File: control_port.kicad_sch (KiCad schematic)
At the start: 14 parts, among them J2 USB_C, U16 PI3USB102G

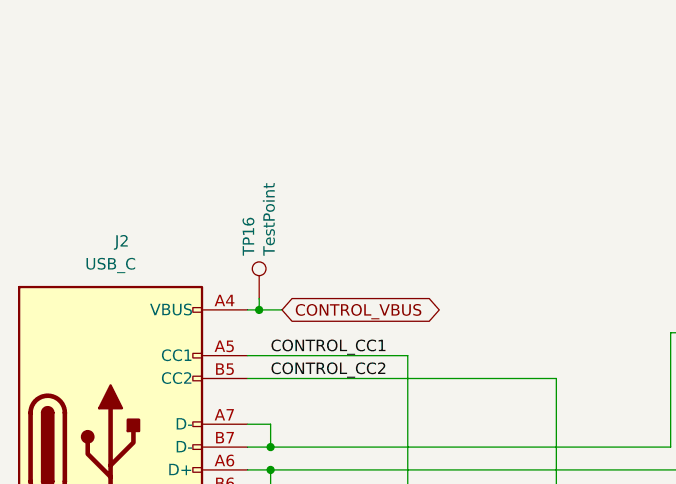
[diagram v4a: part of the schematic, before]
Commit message: Use four-terminal current sense resistor symbol
Previously we had used a special four-terminal symbol and footprint to
ensure that current sense signals did not connect to power supply zones
in multiple places. We rejected this in favor of a two-terminal
schematic symbol and standard resistor footprint to ensure reliable
assembly.

This new solution uses a four-terminal schematic symbol with a
two-terminal footprint which is actually four terminals in two
overlapping pairs using the "net tie" footprint feature.

Fixes #13
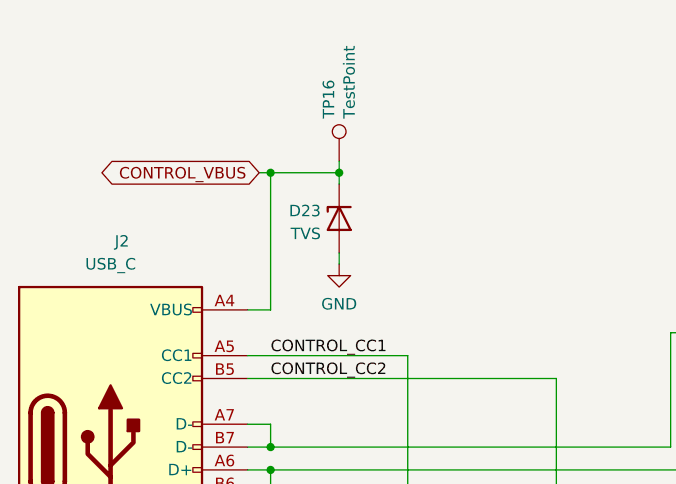
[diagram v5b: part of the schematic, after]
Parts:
- added D23: TVS, cynthion:DFN1006-2, symbol Device:D_Zener
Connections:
- net CONTROL_VBUS: now also D23.1 (K)
- net GND: now also D23.2 (A)
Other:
- moved on the sheet: TP16
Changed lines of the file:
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@@
   (junction (at 77.47 87.63) (diameter 0) (color 0 0 0 0)
   )
+  (junction (at 85.09 54.61) (diameter 0) (color 0 0 0 0)
+  )
   (junction (at 92.71 105.41) (diameter 0) (color 0 0 0 0)
   )
@@
   (junction (at 109.22 105.41) (diameter 0) (color 0 0 0 0)
   )
-  (junction (at 76.2 69.85) (diameter 0) (color 0 0 0 0)
+  (junction (at 77.47 54.61) (diameter 0) (color 0 0 0 0)
   )
   (no_connect (at 74.93 100.33))
@@
     (stroke (width 0) (type default))
   )
-  (wire (pts (xy 76.2 68.58) (xy 76.2 69.85))
+  (wire (pts (xy 77.47 69.85) (xy 74.93 69.85))
+    (stroke (width 0) (type default))
+  )
+  (wire (pts (xy 77.47 54.61) (xy 77.47 69.85))
     (stroke (width 0) (type default))
   )
@@
     (stroke (width 0) (type default))
   )
-  (wire (pts (xy 76.2 69.85) (xy 78.74 69.85))
-    (stroke (width 0) (type default))
-  )
   (wire (pts (xy 231.14 62.23) (xy 231.14 63.5))
     (stroke (width 0) (type default))
@@
     (stroke (width 0) (type default))
   )
-  (wire (pts (xy 74.93 69.85) (xy 76.2 69.85))
-    (stroke (width 0) (type default))
-  )
   (wire (pts (xy 92.71 95.25) (xy 92.71 92.71))
     (stroke (width 0) (type default))
@@
     (stroke (width 0) (type default))
   )
+  (wire (pts (xy 76.2 54.61) (xy 77.47 54.61))
+    (stroke (width 0) (type default))
+  )
   (wire (pts (xy 259.08 81.28) (xy 259.08 82.55))
     (stroke (width 0) (type default))
@@
     (stroke (width 0) (type default))
   )
+  (wire (pts (xy 85.09 64.77) (xy 85.09 63.5))
+    (stroke (width 0) (type default))
+  )
   (wire (pts (xy 198.12 77.47) (xy 199.39 77.47))
     (stroke (width 0) (type default))
   )
+  (wire (pts (xy 77.47 54.61) (xy 85.09 54.61))
+    (stroke (width 0) (type default))
+  )
   (wire (pts (xy 92.71 74.93) (xy 92.71 92.71))
     (stroke (width 0) (type default))
@@
     (stroke (width 0) (type default))
   )
+  (wire (pts (xy 85.09 53.34) (xy 85.09 54.61))
+    (stroke (width 0) (type default))
+  )
   (wire (pts (xy 208.28 129.54) (xy 208.28 130.81))
     (stroke (width 0) (type default))
@@
   )
   (wire (pts (xy 173.99 80.01) (xy 173.99 113.03))
+    (stroke (width 0) (type default))
+  )
+  (wire (pts (xy 85.09 54.61) (xy 85.09 55.88))
     (stroke (width 0) (type default))
   )
@@
     (effects (font (size 1.27 1.27)) (justify left bottom))
   )
-  (global_label "CONTROL_VBUS" (shape bidirectional) (at 78.74 69.85 0) (fields_autoplaced)
-    (effects (font (size 1.27 1.27)) (justify left))
-    (property "Intersheetrefs" "${INTERSHEET_REFS}" (at 95.4575 69.7706 0)
-      (effects (font (size 1.27 1.27)) (justify left) hide)
+  (global_label "CONTROL_VBUS" (shape bidirectional) (at 76.2 54.61 180) (fields_autoplaced)
+    (effects (font (size 1.27 1.27)) (justify right))
+    (property "Intersheetrefs" "${INTERSHEET_REFS}" (at 58.5231 54.61 0)
+      (effects (font (size 1.27 1.27)) (justify right) hide)
     )
   )
@@
         (path "/fb621148-8145-4217-9712-738e1b5a4823/00000000-0000-0000-0000-00005dcd9772"
           (reference "C62") (unit 1)
+        )
+      )
+    )
+  )
+  (symbol (lib_id "Device:D_Zener") (at 85.09 59.69 90) (mirror x) (unit 1)
+    (in_bom yes) (on_board yes) (dnp no) (fields_autoplaced)
+    (property "Reference" "D23" (at 83.058 58.8553 90)
+      (effects (font (size 1.27 1.27)) (justify left))
+    )
+    (property "Value" "TVS" (at 83.058 61.3922 90)
+      (effects (font (size 1.27 1.27)) (justify left))
+    )
+    (property "Footprint" "cynthion:DFN1006-2" (at 85.09 59.69 0)
+      (effects (font (size 1.27 1.27)) hide)
+    )
+    (property "Datasheet" "https://assets.nexperia.com/documents/data-sheet/PESDXS1UL_SER.pdf" (at 85.09 59.69 0)
+      (effects (font (size 1.27 1.27)) hide)
+    )
+    (property "Manufacturer" "Nexperia" (at 85.09 59.69 90)
+      (effects (font (size 1.27 1.27)) hide)
+    )
+    (property "Part Number" "PESD36VS1UL,315" (at 85.09 59.69 90)
+      (effects (font (size 1.27 1.27)) hide)
+    )
+    (property "Description" "TVS DIODE 36VWM 80VC DFN1006-2" (at 85.09 59.69 0)
+      (effects (font (size 1.27 1.27)) hide)
+    )
+    (pin "1")
+    (pin "2")
+    (instances
+      (project "cynthion"
+        (path "/fb621148-8145-4217-9712-738e1b5a4823/490fda6e-4eae-4b35-a875-405b51914829"
+          (reference "D23") (unit 1)
+        )
+        (path "/fb621148-8145-4217-9712-738e1b5a4823/00000000-0000-0000-0000-00005dcd9772"
+          (reference "D23") (unit 1)
         )
       )
@@
     )
   )
-  (symbol (lib_id "Connector:TestPoint") (at 76.2 68.58 0) (unit 1)
+  (symbol (lib_id "Connector:TestPoint") (at 85.09 53.34 0) (unit 1)
     (in_bom no) (on_board yes) (dnp no)
-    (property "Reference" "TP16" (at 75.057 63.8302 90)
-      (effects (font (size 1.27 1.27)) (justify left))
-    )
-    (property "Value" "TestPoint" (at 77.343 63.8302 90)
-      (effects (font (size 1.27 1.27)) (justify left))
-    )
-    (property "Footprint" "TestPoint:TestPoint_Pad_D1.0mm" (at 81.28 68.58 0)
-      (effects (font (size 1.27 1.27)) hide)
-    )
-    (property "Datasheet" "~" (at 81.28 68.58 0)
+    (property "Reference" "TP16" (at 83.947 48.5902 90)
+      (effects (font (size 1.27 1.27)) (justify left))
+    )
+    (property "Value" "TestPoint" (at 86.233 48.5902 90)
+      (effects (font (size 1.27 1.27)) (justify left))
+    )
+    (property "Footprint" "TestPoint:TestPoint_Pad_D1.0mm" (at 90.17 53.34 0)
+      (effects (font (size 1.27 1.27)) hide)
+    )
+    (property "Datasheet" "~" (at 90.17 53.34 0)
       (effects (font (size 1.27 1.27)) hide)
     )
@@
         )
       )
+    )
+  )
+  (symbol (lib_id "power:GND") (at 85.09 64.77 0) (unit 1)
+    (in_bom yes) (on_board yes) (dnp no) (fields_autoplaced)
+    (property "Reference" "#PWR025" (at 85.09 71.12 0)
+      (effects (font (size 1.27 1.27)) hide)
+    )
+    (property "Value" "GND" (at 85.09 69.2134 0)
+      (effects (font (size 1.27 1.27)))
+    )
+    (property "Footprint" "" (at 85.09 64.77 0)
+      (effects (font (size 1.27 1.27)) hide)
+    )
+    (property "Datasheet" "" (at 85.09 64.77 0)
+      (effects (font (size 1.27 1.27)) hide)
+    )
+    (pin "1")
+    (instances
+      (project "cynthion"
+        (path "/fb621148-8145-4217-9712-738e1b5a4823/490fda6e-4eae-4b35-a875-405b51914829"
+          (reference "#PWR025") (unit 1)
+        )
+        (path "/fb621148-8145-4217-9712-738e1b5a4823/00000000-0000-0000-0000-00005dcd9772"
+          (reference "#PWR025") (unit 1)
+        )
+      )

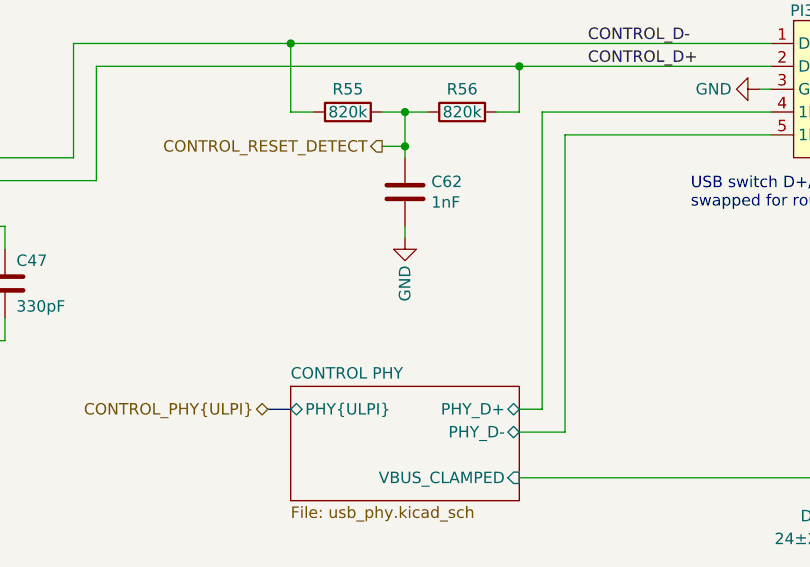
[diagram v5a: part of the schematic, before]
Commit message: Clean up schematic
- Renumber Pmod signal names to match silkscreen labels
- Clean up FPGA symbol
- Clean up PHY symbol
- Add title block to newer sheets
- Fix horizontal line in LED sheet
- Improve various label positions
- Update data sheet fields
- Renumber pages
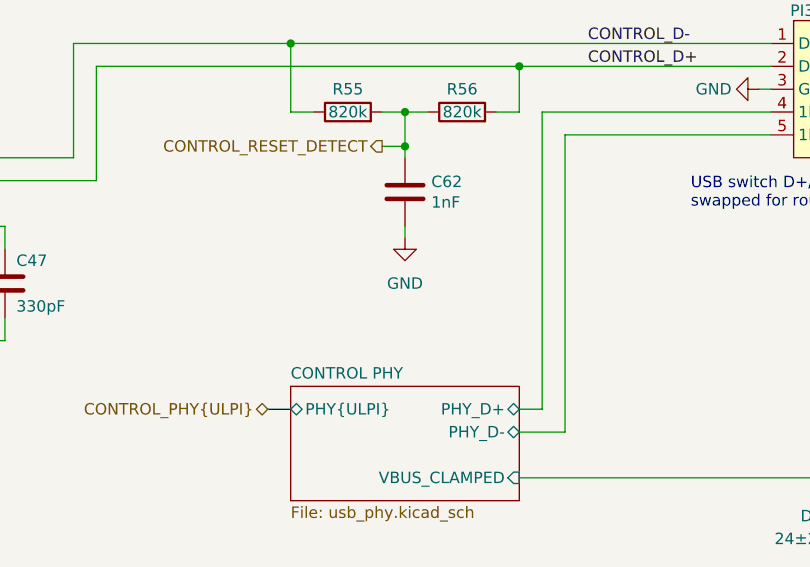
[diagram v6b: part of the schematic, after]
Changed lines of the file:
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@@
       (effects (font (size 1.27 1.27)) hide)
     )
-    (property "Value" "GND" (at 158.75 99.06 90)
+    (property "Value" "GND" (at 158.75 99.06 0)
       (effects (font (size 1.27 1.27)))
     )
@@
   )
   (symbol (lib_id "power:GND") (at 208.28 130.81 0) (mirror y) (unit 1)
-    (in_bom yes) (on_board yes) (dnp no) (fields_autoplaced)
+    (in_bom yes) (on_board yes) (dnp no)
     (property "Reference" "#PWR0156" (at 208.28 137.16 0)
       (effects (font (size 1.27 1.27)) hide)
@@
     (instances
       (project "cynthion"
-        (path "/fb621148-8145-4217-9712-738e1b5a4823/00000000-0000-0000-0000-00005dcd9772" (page "12"))
-      )
-    )
+        (path "/fb621148-8145-4217-9712-738e1b5a4823/00000000-0000-0000-0000-00005dcd9772" (page "3"))
+      )
+    )

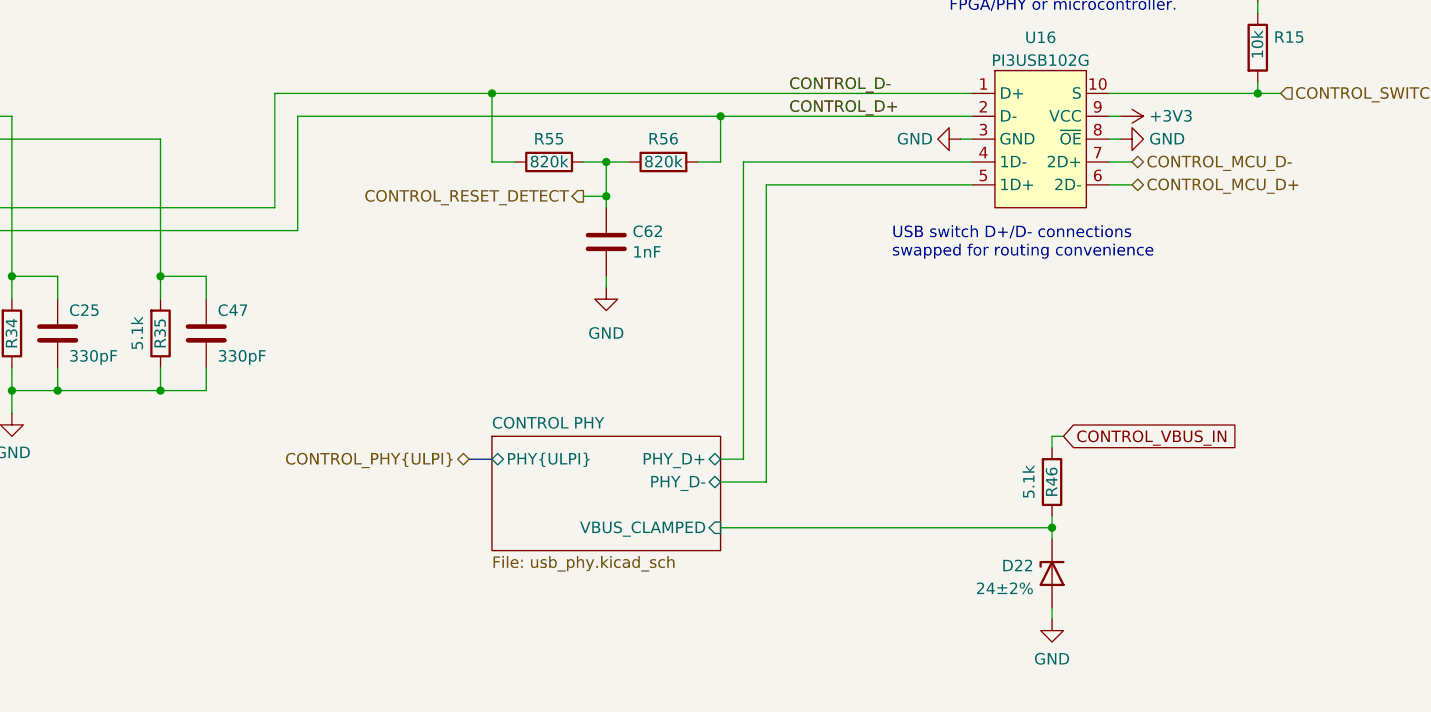
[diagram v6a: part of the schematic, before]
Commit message: Add second common-mode choke for TARGET port
Instead of having a single choke connected in series with the PHY, we
now have a choke in series with each connector. The PHY is connected
between the two chokes.
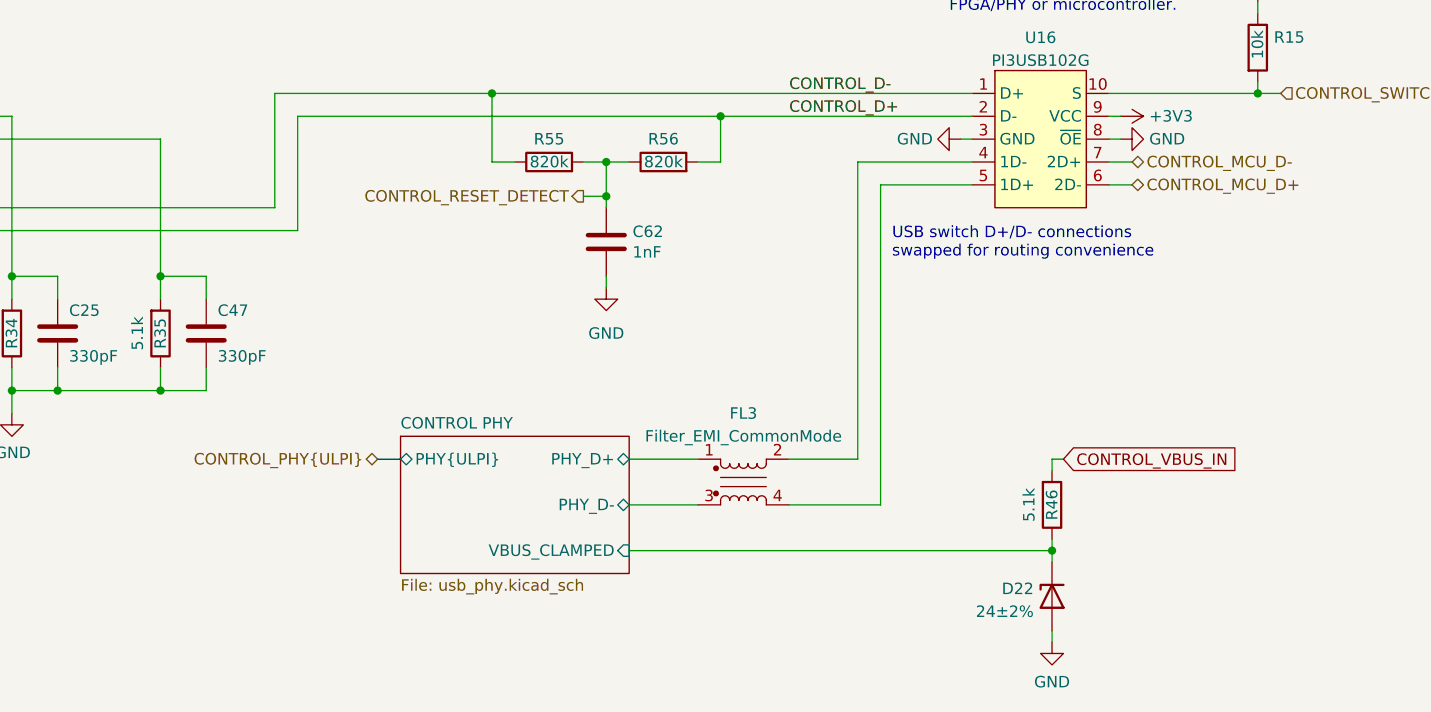
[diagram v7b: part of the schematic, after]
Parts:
- added FL3: Filter_EMI_CommonMode, cynthion:L_CommonModeChoke_Murata_DLM0NS, symbol Device:Filter_EMI_CommonMode
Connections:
- net CONTROL PHY/PHY_D+: now also FL3.1; no longer U16.4 (1D-)
- net CONTROL PHY/PHY_D-: now also FL3.3; no longer U16.5 (1D+)
- new net: FL3.2, U16.4 (1D-)
- new net: FL3.4, U16.5 (1D+)
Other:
- moved on the sheet: D22, R46
